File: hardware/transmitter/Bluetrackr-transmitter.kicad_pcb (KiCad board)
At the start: 2 copper layers, 50.8 x 30.5 mm, 43 parts, among them J1 USB_C_Receptacle_USB2.0, J2 Programming_Connector, J3 Battery_Connector, Q1 CJ2333, SW1 SW_Pair, U1 MIC5205-2.5YM5, U2 MCP73831-2-OT, U3 STM32F072C8Tx, U4 DL-24N-2.4G, U5 LSM9DS1

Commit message: Place Power components
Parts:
- C5, C6, R4, U2: moved to F.Cu
- moved R2 101.8 mm to (143.5, 100.8), turned to 90 degrees
- moved D1 86.6 mm to (146.3, 100.1), turned to 180 degrees
- moved Q1 84.9 mm to (146.3, 102.9), turned to 0 degrees
- moved C3 82.9 mm to (146.3, 98.0), turned to 180 degrees
- moved R1 82.2 mm to (113.0, 95.6)
- moved C1 81.2 mm to (151.4, 98.0)
- moved C2 81.2 mm to (154.4, 101.1)
- moved C4 81.2 mm to (151.4, 104.1)
- moved U1 81.2 mm to (151.4, 101.1)
- moved R3 60.7 mm to (113.0, 99.3), turned to -90 degrees
- moved C5 25.9 mm to (140.5, 97.7)
- moved R4 23.1 mm to (137.4, 98.7), turned to 90 degrees
- moved C6 16.5 mm to (140.4, 104.0)
- moved U2 13.9 mm to (140.5, 100.8), turned to 90 degrees
- moved C15 8.36 mm to (152.0, 78.4), turned to 0 degrees
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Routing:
- net /NRF_MOSI: track 0.00 -> 19.6 mm
- net VCC: track 0.00 -> 12.9 mm
- net +2V5: track 0.00 -> 2.13 mm
- net Net-(C4-Pad1): track 0.00 -> 1.98 mm

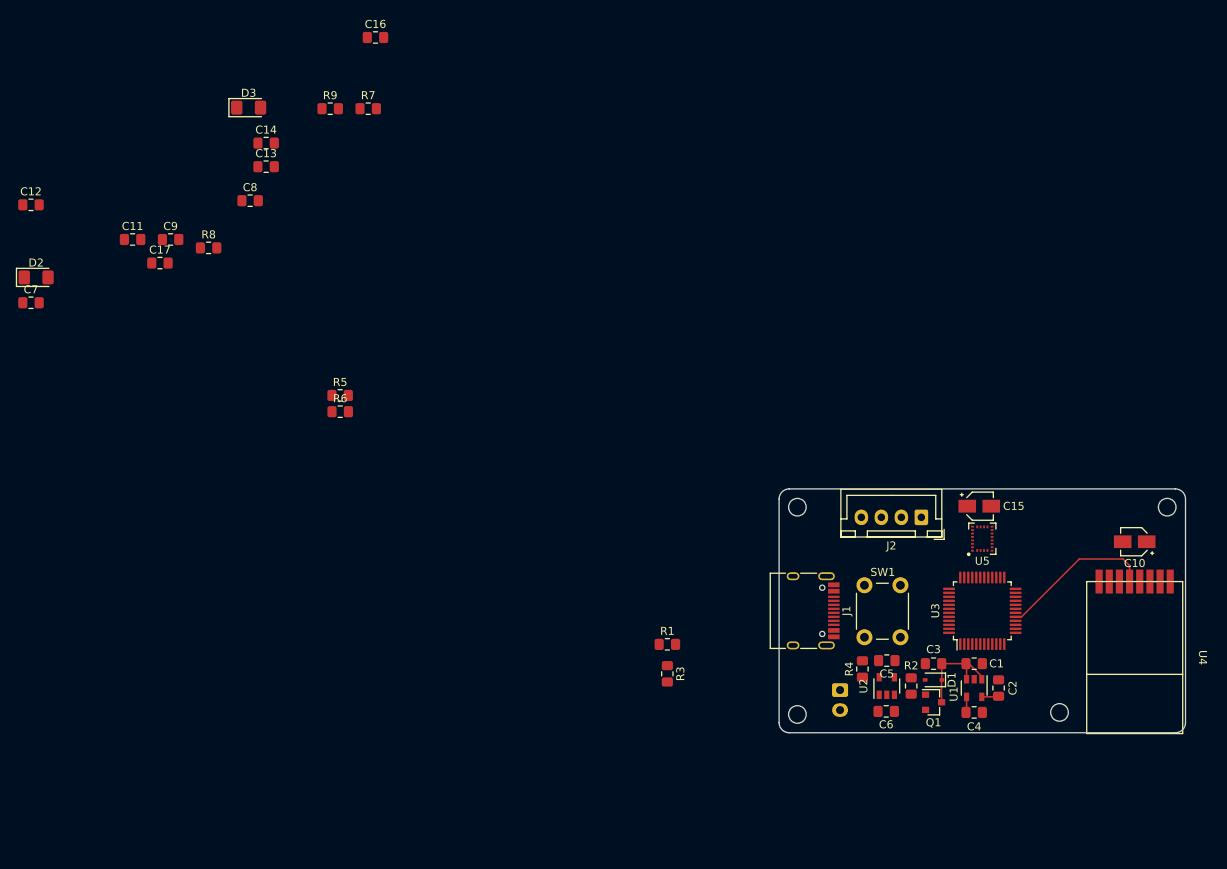
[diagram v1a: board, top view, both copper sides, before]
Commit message: Place CC1 and CC2 for USB
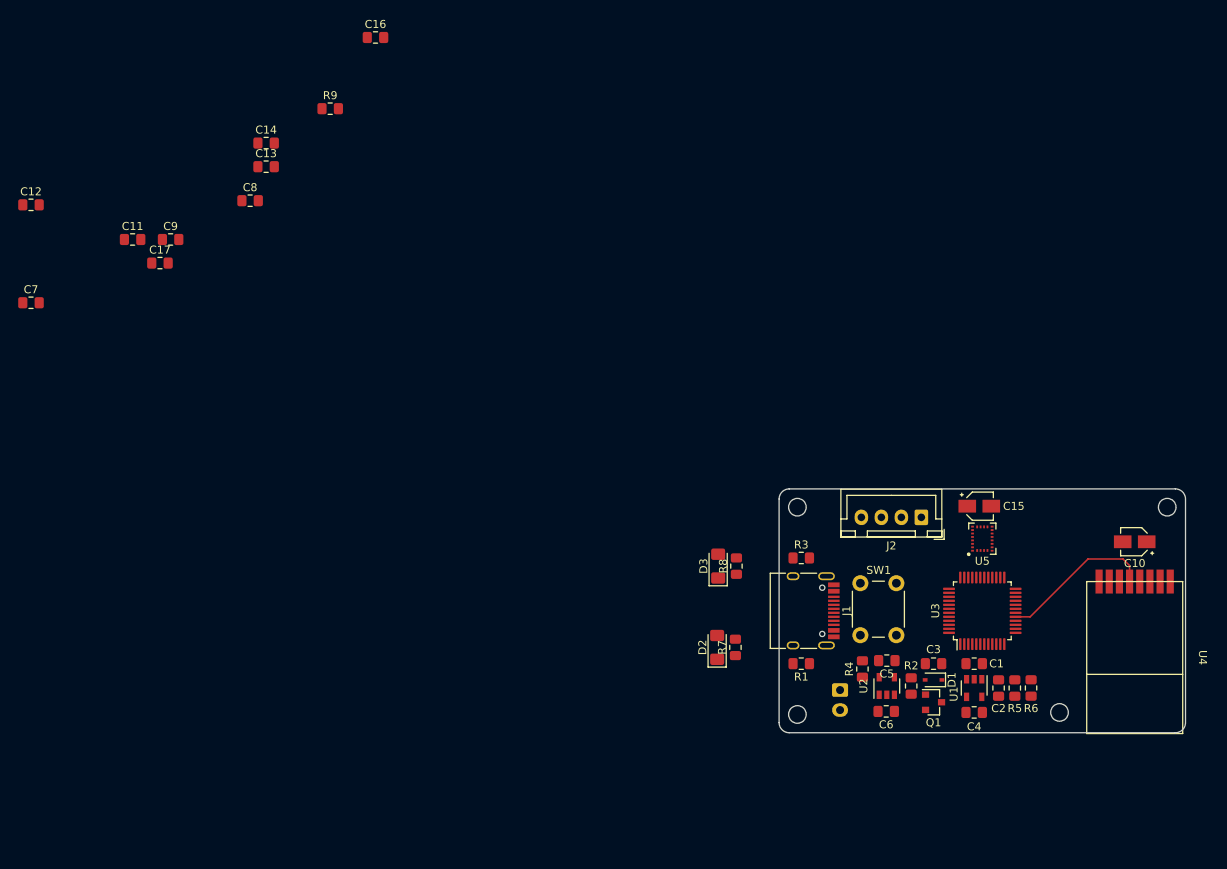
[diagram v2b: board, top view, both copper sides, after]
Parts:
- moved D2 96.9 mm to (119.3, 96.0), turned to 90 degrees
- moved R6 93.0 mm to (158.5, 101.1), turned to 90 degrees
- moved R5 91.9 mm to (156.5, 101.1), turned to -90 degrees
- moved D3 82.0 mm to (119.4, 85.9), turned to 90 degrees
- moved R7 81.5 mm to (121.5, 96.0), turned to 90 degrees
- moved R8 77.0 mm to (121.7, 85.9), turned to 90 degrees
- moved R3 22.1 mm to (129.8, 84.8), turned to 180 degrees
- moved R1 16.9 mm to (129.8, 98.0), turned to 180 degrees
- moved SW1 0.57 mm to (137.2, 94.5)
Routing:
- net VCC: track 12.9 -> 0.00 mm
- net +2V5: track 2.13 -> 0.00 mm
- net Net-(C4-Pad1): track 1.98 -> 0.00 mm

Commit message: Place LEDs
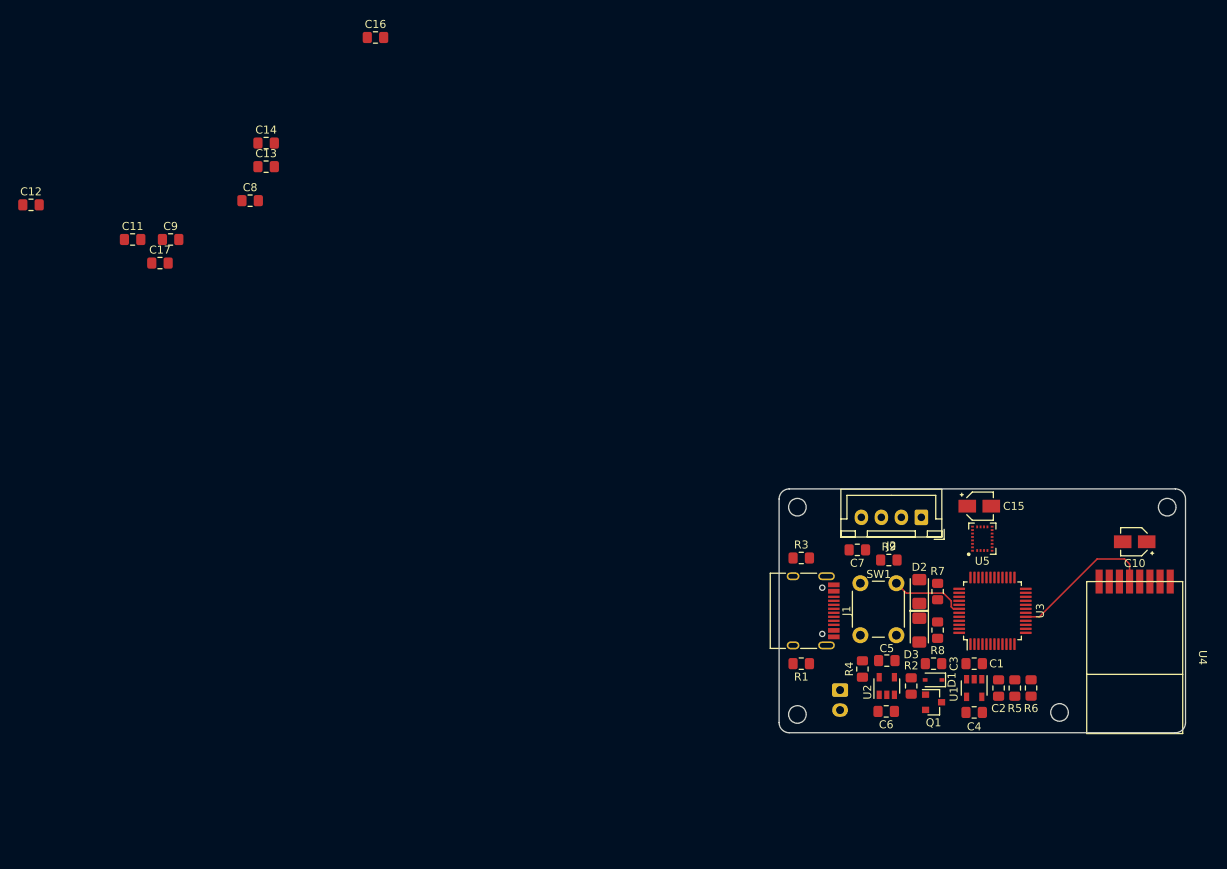
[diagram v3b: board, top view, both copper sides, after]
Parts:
- moved C7 107.8 mm to (136.8, 83.8), turned to 180 degrees
- moved R9 89.8 mm to (140.7, 85.1)
- moved D3 26.4 mm to (144.5, 93.9), turned to -90 degrees
- moved R8 26.4 mm to (146.8, 93.9), turned to -90 degrees
- moved D2 26.2 mm to (144.5, 89.0)
- moved R7 26.2 mm to (146.8, 89.0)
- moved U3 1.27 mm to (153.7, 91.4)
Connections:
- net /USB_DM renamed /USB_D-
- net /USB_DP renamed /USB_D+
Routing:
- net /BTN_PAIR: track 0.00 -> 9.61 mm
- net /NRF_MOSI: track 19.6 -> 18.4 mm

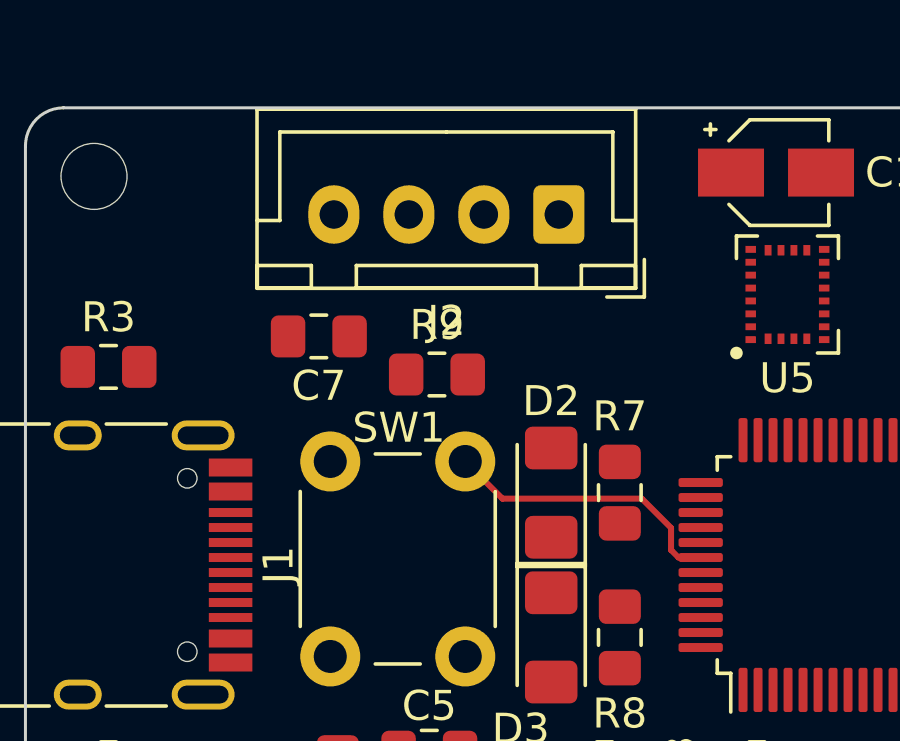
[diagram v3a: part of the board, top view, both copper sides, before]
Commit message: Place BOOT0 resistor
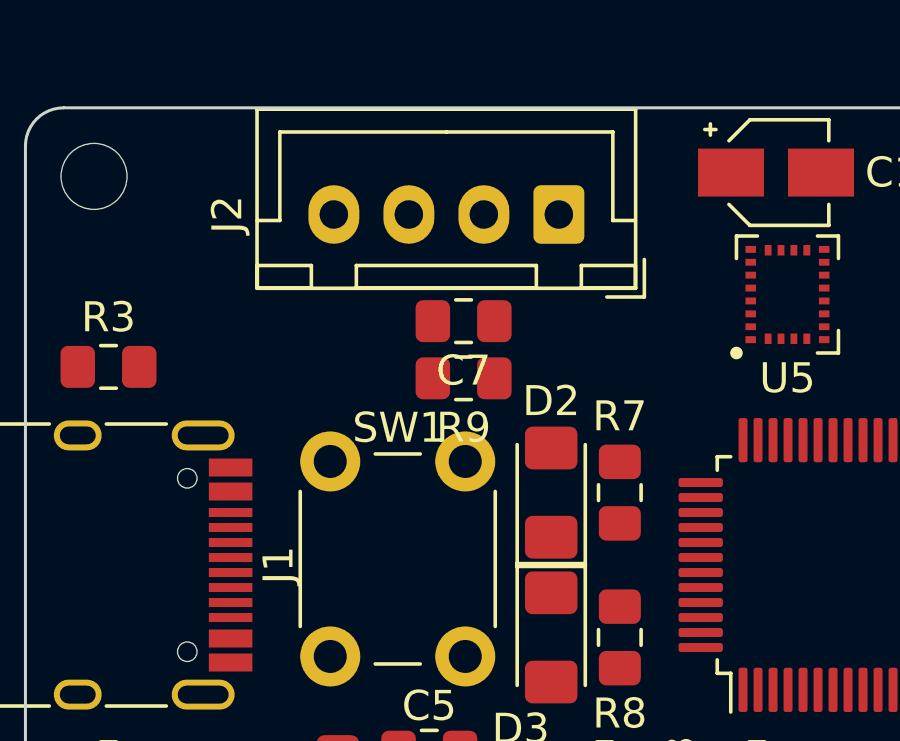
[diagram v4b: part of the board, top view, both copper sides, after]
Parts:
- moved C7 4.85 mm to (141.6, 83.3)
- moved R9 0.90 mm to (141.6, 85.2), turned to 180 degrees
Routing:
- net /BTN_PAIR: track 9.61 -> 0.00 mm
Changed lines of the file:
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@@
     (thickness 1.6)
     (drawings 13)
-    (tracks 11)
+    (tracks 5)
     (modules 43)
     (nets 56)
@@
   )
   (module "Resistor_SMD:R_0805_2012Metric_Pad1.15x1.40mm_HandSolder" (layer "F.Cu")
-    (at 140.716 85.09)
+    (at 141.605 85.217 180)
     (descr "Resistor SMD 0805 (2012 Metric), square (rectangular) end terminal, IPC_7351 nominal with elongated pad for handsoldering. (Body size source: https://docs.google.com/spreadsheets/d/1BsfQQcO9C6DZCsRaXUlFlo91Tg2WpOkGARC1WS5S8t0/edit?usp=sharing), generated with kicad-footprint-generator")
     (tags "resistor handsolder")
@@
     (fp_line (start -1 -0.6) (end 1 -0.6) (layer "F.Fab") (width 0.1))
     (fp_line (start -1 0.6) (end -1 -0.6) (layer "F.Fab") (width 0.1))
-    (pad "2" smd roundrect (at 1.025 0) (size 1.15 1.4) (layers "F.Cu" "F.Paste" "F.Mask") (roundrect_rratio 0.217391)
-      (net 1 "GND"))
-    (pad "1" smd roundrect (at -1.025 0) (size 1.15 1.4) (layers "F.Cu" "F.Paste" "F.Mask") (roundrect_rratio 0.217391)
+    (pad "2" smd roundrect (at 1.025 0 180) (size 1.15 1.4) (layers "F.Cu" "F.Paste" "F.Mask") (roundrect_rratio 0.217391)
+      (net 1 "GND"))
+    (pad "1" smd roundrect (at -1.025 0 180) (size 1.15 1.4) (layers "F.Cu" "F.Paste" "F.Mask") (roundrect_rratio 0.217391)
       (net 22 "Net-(R9-Pad1)"))
     (model "${KISYS3DMOD}/Resistor_SMD.3dshapes/R_0805_2012Metric.wrl"
@@
     (descr "JST XH series connector, B4B-XH-A (http://www.jst-mfg.com/product/pdf/eng/eXH.pdf), generated with kicad-footprint-generator")
     (tags "connector JST XH vertical")
-    (fp_text reference "J2" (at 3.75 -3.55) (layer "F.SilkS")
+    (fp_text reference "J2" (at 11.049 0 90) (layer "F.SilkS")
       (effects (font (size 1 1) (thickness 0.15)))
     )
@@
   )
   (module "Capacitor_SMD:C_0805_2012Metric_Pad1.15x1.40mm_HandSolder" (layer "F.Cu")
-    (at 136.779 83.82 180)
+    (at 141.605 83.312 180)
     (descr "Capacitor SMD 0805 (2012 Metric), square (rectangular) end terminal, IPC_7351 nominal with elongated pad for handsoldering. (Body size source: https://docs.google.com/spreadsheets/d/1BsfQQcO9C6DZCsRaXUlFlo91Tg2WpOkGARC1WS5S8t0/edit?usp=sharing), generated with kicad-footprint-generator")
     (tags "capacitor handsolder")
@@
     (arrow2b (pts (xy 127 76.2) (xy 128.126504 75.613579)))
   )
-  (segment (start 141.66 87.988) (end 142.89899 89.22699) (width 0.2) (layer "F.Cu") (net 23))
-  (segment (start 142.89899 89.22699) (end 147.54449 89.22699) (width 0.2) (layer "F.Cu") (net 23))
-  (segment (start 148.77 91.19) (end 149.5075 91.19) (width 0.2) (layer "F.Cu") (net 23))
-  (segment (start 147.54449 89.22699) (end 148.51999 90.20249) (width 0.2) (layer "F.Cu") (net 23))
-  (segment (start 148.51999 90.20249) (end 148.51999 90.93999) (width 0.2) (layer "F.Cu") (net 23))
-  (segment (start 148.51999 90.93999) (end 148.77 91.19) (width 0.2) (layer "F.Cu") (net 23))
   (segment (start 170.81 85.593) (end 170.18 84.963) (width 0.2) (layer "F.Cu") (net 36))
   (segment (start 170.81 87.782) (end 170.81 85.593) (width 0.2) (layer "F.Cu") (net 36))

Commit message: Change connectors to ZH SMD versions
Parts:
- C13: moved to B.Cu
- moved C12 124.1 mm to (149.0, 86.1), turned to 90 degrees
- moved C9 118.1 mm to (156.5, 98.0)
- moved C11 114.5 mm to (148.6, 96.3), turned to 180 degrees
- moved C8 108.0 mm to (158.6, 86.1), turned to 90 degrees
- moved C14 105.5 mm to (163.8, 63.6)
- moved C17 105.1 mm to (149.0, 82.3), turned to 90 degrees
- moved C13 94.9 mm to (145.7, 82.3), turned to 180 degrees
- moved C16 93.2 mm to (149.0, 78.4), turned to 90 degrees
- moved C7 4.47 mm to (137.3, 84.5), turned to -90 degrees
- moved C15 2.04 mm to (154.1, 78.2)
- moved R9 0.77 mm to (141.7, 84.5), turned to 90 degrees
- moved R8 0.38 mm to (146.8, 93.5)
- moved R7 0.37 mm to (146.8, 89.4)

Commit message: Add 3D models to JST ZH connectors
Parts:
- J2: footprint Connector_JST:JST_XH_B4B-XH-A_1x04_P2.50mm_Vertical -> User_Connector_JST:JST_B4B-ZR-SM4-TF
- J3: footprint Connector_JST:JST_XH_S2B-XH-A_1x02_P2.50mm_Horizontal -> User_Connector_JST:JST_S2B-ZR-SM4A-TF
- moved J2 6.77 mm to (138.0, 80.5)
- moved J3 1.26 mm to (135.5, 102.2)

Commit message: Begin routing
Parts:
- C14: moved to B.Cu
- moved C14 27.6 mm to (145.7, 84.5), turned to 180 degrees
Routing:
- net /NRST: track 0.00 -> 28.1 mm, vias 0 -> 2
- net /USB_D-: track 0.00 -> 27.6 mm
- net /USB_D+: track 0.00 -> 27.5 mm
- net /NRF_CE: track 0.00 -> 20.8 mm
- net /SWDIO: track 0.00 -> 19.6 mm, vias 0 -> 2
- net /NRF_CSN: track 0.00 -> 19.4 mm
- net /SWCLK: track 0.00 -> 17.9 mm, vias 0 -> 2
- net /NRF_SCLK: track 0.00 -> 17.9 mm
- net /NRF_INT: track 0.00 -> 16.5 mm, vias 0 -> 2
- net Net-(R9-Pad1): track 0.00 -> 15.6 mm
- net /NRF_MISO: track 0.00 -> 15.1 mm
- net /BTN_PAIR: track 0.00 -> 9.82 mm
- net Net-(J1-PadA5): track 0.00 -> 7.16 mm
- net Net-(J1-PadB5): track 0.00 -> 6.79 mm
- net /LED_STATUS: track 0.00 -> 3.95 mm
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
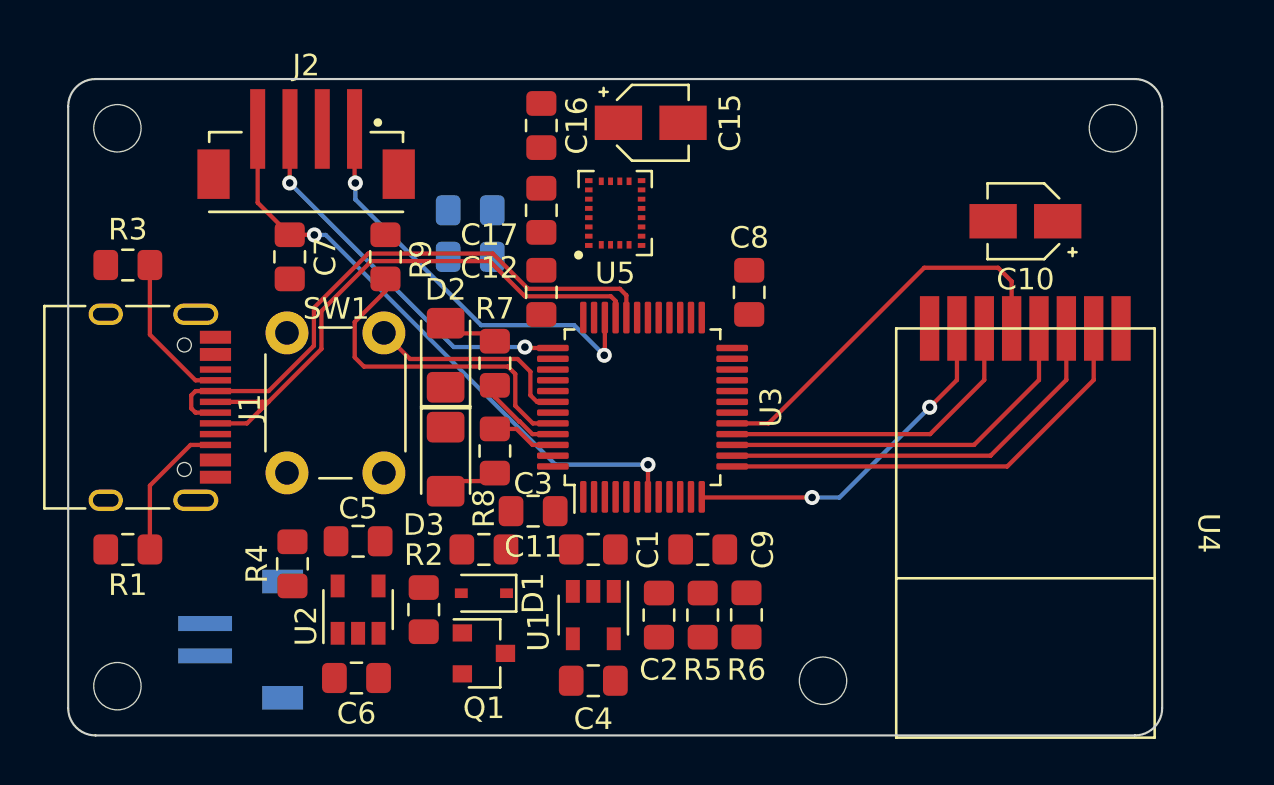
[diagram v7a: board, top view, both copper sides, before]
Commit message: Routed USB, SPI tracks
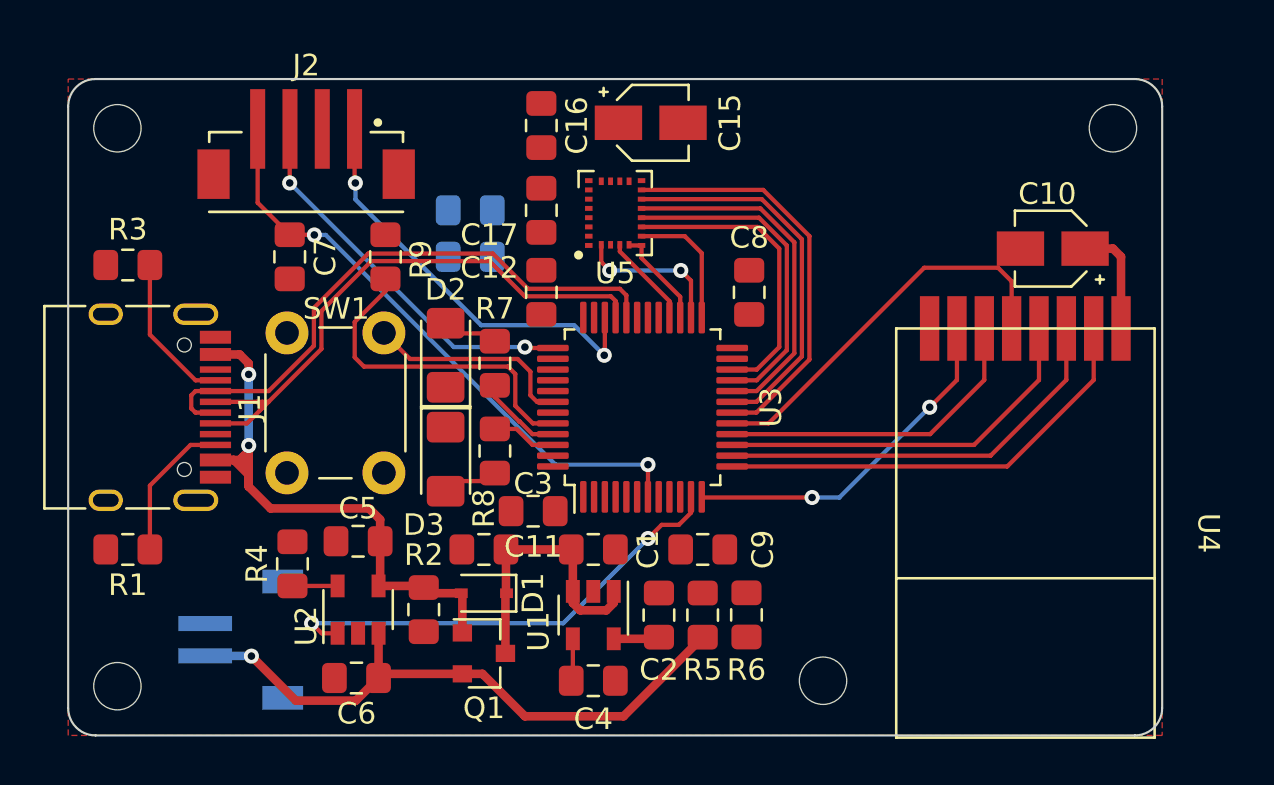
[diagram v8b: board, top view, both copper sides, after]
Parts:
- moved C10 1.80 mm to (172.7, 84.1)
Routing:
- net +BATT: track 0.00 -> 28.9 mm, vias 0 -> 1
- net VBUS: track 0.00 -> 28.1 mm, vias 0 -> 2
- net /CHARGE_STATUS: track 0.00 -> 21.9 mm, vias 0 -> 2
- net /IMU_INT2_AG: track 0.00 -> 19.0 mm
- net /IMU_INT1_AG: track 0.00 -> 17.8 mm
- net /IMU_INT_M: track 0.00 -> 16.5 mm
- net /IMU_RDY_M: track 0.00 -> 15.3 mm
- net /IMU_CS_M: track 0.00 -> 14.0 mm
- net VCC: track 0.00 -> 13.1 mm
- net +2V5: track 0.00 -> 7.29 mm
- net /IMU_SCLK: track 0.00 -> 7.04 mm, vias 0 -> 2
- net /IMU_CS_AG: track 0.00 -> 6.11 mm
- net /IMU_MISO: track 0.00 -> 4.69 mm
- net /IMU_MOSI: track 0.00 -> 4.33 mm
- net Net-(R4-Pad1): track 0.00 -> 2.10 mm
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- added copper zone on F.Cu, net GND
